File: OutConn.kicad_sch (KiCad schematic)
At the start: 0 parts

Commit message: Adding 5v and 3v3 buck
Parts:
- added J?: 2041441-1, TE_2041441-1, symbol 2041441-1:DP_CONN
- added J?: USB_A_Stacked, symbol Connector:USB_A_Stacked
- added R?: 5M, symbol Device:R_US
- added R?: 1M, symbol Device:R_US
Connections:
- new net: J?.14 (CFG2), R?.1
- new net: J?.13 (CFG1), R?.1
- new net +3V3: J?.20 (DP_PWR)
- new net +5V: J?.1 (VBUS1), J?.5 (VBUS2)
- new net GND: J?.11 (GND), J?.16 (GND), J?.19 (RTN), J?.2 (GND), J?.4 (GND1), J?.5 (GND), J?.8 (GND), J?.8 (GND2), J?.9 (Shield), J?.SH1 (SHIELD), J?.SH2 (SHIELD), J?.SH3 (SHIELD), R?.2, R?.2
- new net SINK_DP.AUX_M: J?.17 (AUX_N)
- new net SINK_DP.AUX_P: J?.15 (AUX_P)
- new net SINK_DP.D0_M: J?.3 (ML0_M)
- new net SINK_DP.D0_P: J?.1 (ML0_P)
- new net SINK_DP.D1_M: J?.6 (ML1_N)
- new net SINK_DP.D1_P: J?.4 (ML1_P)
- new net SINK_DP.D2_M: J?.9 (ML2_M)
- new net SINK_DP.D2_P: J?.7 (ML2_P)
- new net SINK_DP.D3_M: J?.12 (ML3_N)
- new net SINK_DP.D3_P: J?.10 (ML3_P)
- new net SINK_DP.HPD: J?.18 (HPD)
- new net UFP_USB1.D_M: J?.2 (D1-)
- new net UFP_USB1.D_P: J?.3 (D1+)
- new net UFP_USB2.D_M: J?.6 (D2-)
- new net UFP_USB2.D_P: J?.7 (D2+)

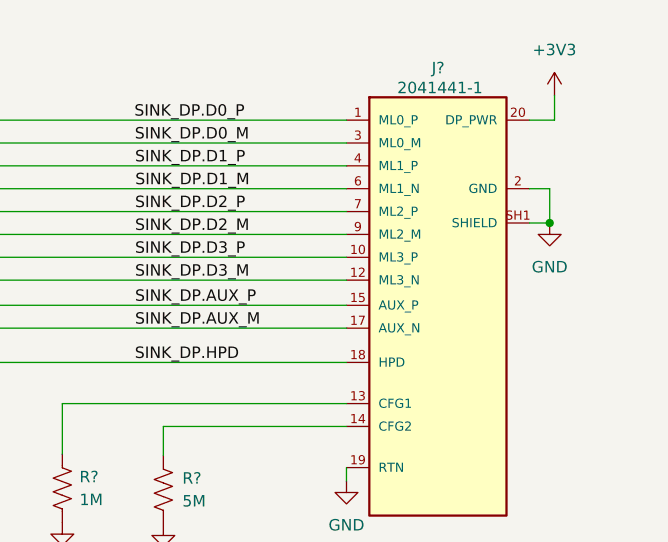
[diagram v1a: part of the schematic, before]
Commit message: fixing sheet numbers and adding schematic PDF
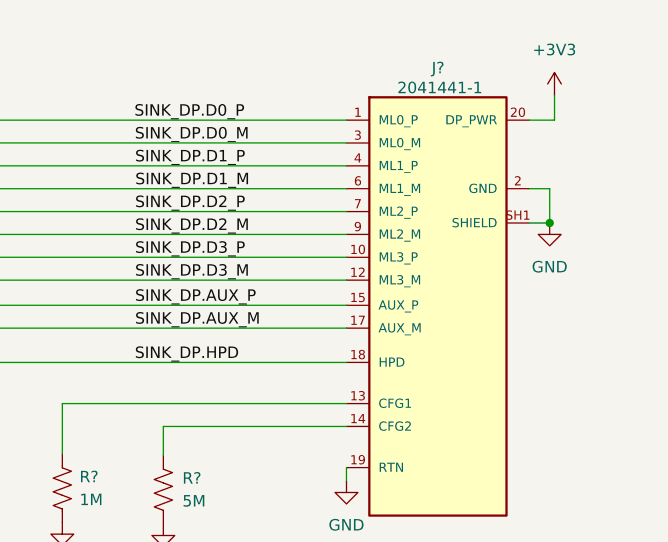
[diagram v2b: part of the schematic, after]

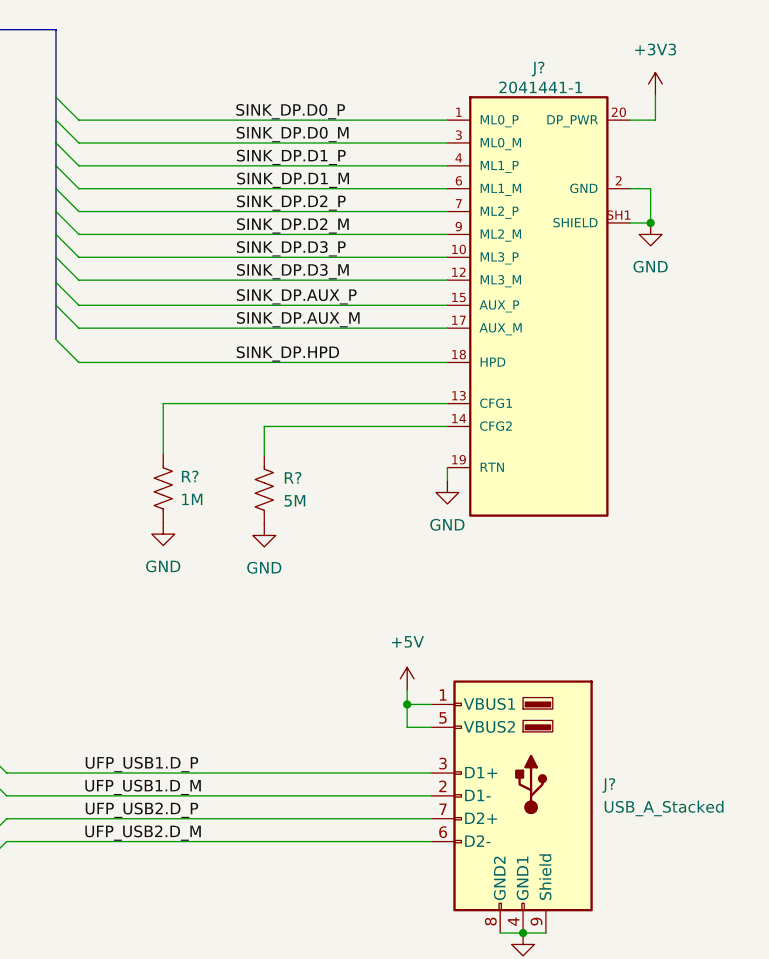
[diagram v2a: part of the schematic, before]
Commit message: Fixing ERC
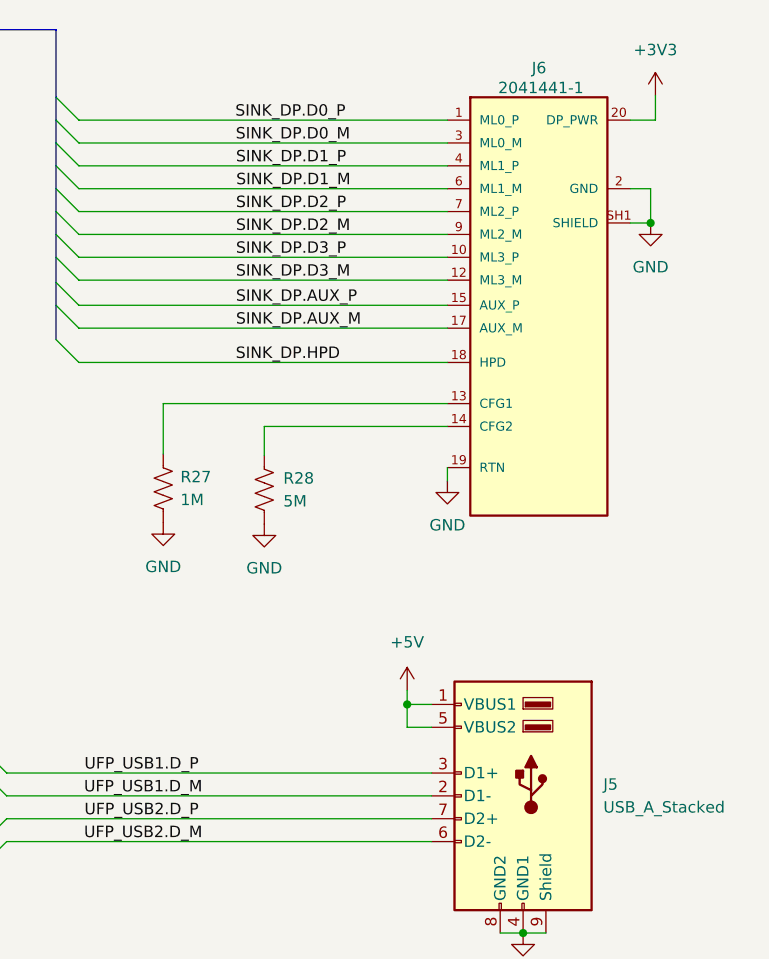
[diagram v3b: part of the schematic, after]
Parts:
- gave numbers to parts that had none: 4
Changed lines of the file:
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@@
   (symbol (lib_id "Device:R_US") (at 122.3518 117.4496 0) (unit 1)
     (in_bom yes) (on_board yes) (fields_autoplaced)
-    (property "Reference" "R?" (id 0) (at 124.46 116.1795 0)
+    (property "Reference" "R28" (id 0) (at 124.46 116.1795 0)
       (effects (font (size 1.27 1.27)) (justify left))
     )
@@
   (symbol (lib_id "power:+5V") (at 138.2268 139.7254 0) (unit 1)
     (in_bom yes) (on_board yes) (fields_autoplaced)
-    (property "Reference" "#PWR?" (id 0) (at 138.2268 143.5354 0)
+    (property "Reference" "#PWR050" (id 0) (at 138.2268 143.5354 0)
       (effects (font (size 1.27 1.27)) hide)
     )
@@
   (symbol (lib_id "power:GND") (at 151.1046 166.7002 0) (mirror y) (unit 1)
     (in_bom yes) (on_board yes) (fields_autoplaced)
-    (property "Reference" "#PWR?" (id 0) (at 151.1046 173.0502 0)
+    (property "Reference" "#PWR052" (id 0) (at 151.1046 173.0502 0)
       (effects (font (size 1.27 1.27)) hide)
     )
@@
   (symbol (lib_id "power:+3V3") (at 165.8112 73.6346 0) (unit 1)
     (in_bom yes) (on_board yes) (fields_autoplaced)
-    (property "Reference" "#PWR?" (id 0) (at 165.8112 77.4446 0)
+    (property "Reference" "#PWR054" (id 0) (at 165.8112 77.4446 0)
       (effects (font (size 1.27 1.27)) hide)
     )
@@
   (symbol (lib_id "2041441-1:DP_CONN") (at 152.8572 96.9518 0) (unit 1)
     (in_bom yes) (on_board yes)
-    (property "Reference" "J?" (id 0) (at 152.8826 70.5866 0))
+    (property "Reference" "J6" (id 0) (at 152.8826 70.5866 0))
     (property "Value" "2041441-1" (id 1) (at 153.0858 72.7964 0))
     (property "Footprint" "TE_2041441-1" (id 2) (at 152.8572 91.6178 0)
@@
   (symbol (lib_id "Device:R_US") (at 111.125 117.2972 0) (unit 1)
     (in_bom yes) (on_board yes) (fields_autoplaced)
-    (property "Reference" "R?" (id 0) (at 113.03 116.0271 0)
+    (property "Reference" "R27" (id 0) (at 113.03 116.0271 0)
       (effects (font (size 1.27 1.27)) (justify left))
     )
@@
   (symbol (lib_id "Connector:USB_A_Stacked") (at 151.1046 151.4602 0) (mirror y) (unit 1)
     (in_bom yes) (on_board yes) (fields_autoplaced)
-    (property "Reference" "J?" (id 0) (at 160.02 150.1901 0)
+    (property "Reference" "J5" (id 0) (at 160.02 150.1901 0)
       (effects (font (size 1.27 1.27)) (justify right))
     )
@@
   (symbol (lib_id "power:GND") (at 165.2778 87.8078 0) (unit 1)
     (in_bom yes) (on_board yes) (fields_autoplaced)
-    (property "Reference" "#PWR?" (id 0) (at 165.2778 94.1578 0)
+    (property "Reference" "#PWR053" (id 0) (at 165.2778 94.1578 0)
       (effects (font (size 1.27 1.27)) hide)
     )
@@
   (symbol (lib_id "power:GND") (at 122.3518 121.2596 0) (unit 1)
     (in_bom yes) (on_board yes) (fields_autoplaced)
-    (property "Reference" "#PWR?" (id 0) (at 122.3518 127.6096 0)
+    (property "Reference" "#PWR049" (id 0) (at 122.3518 127.6096 0)
       (effects (font (size 1.27 1.27)) hide)
     )
@@
   (symbol (lib_id "power:GND") (at 142.6972 116.4844 0) (unit 1)
     (in_bom yes) (on_board yes) (fields_autoplaced)
-    (property "Reference" "#PWR?" (id 0) (at 142.6972 122.8344 0)
+    (property "Reference" "#PWR051" (id 0) (at 142.6972 122.8344 0)
       (effects (font (size 1.27 1.27)) hide)
     )
@@
   (symbol (lib_id "power:GND") (at 111.125 121.1072 0) (unit 1)
     (in_bom yes) (on_board yes) (fields_autoplaced)
-    (property "Reference" "#PWR?" (id 0) (at 111.125 127.4572 0)
+    (property "Reference" "#PWR048" (id 0) (at 111.125 127.4572 0)
       (effects (font (size 1.27 1.27)) hide)
     )

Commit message: Pushing what i have now
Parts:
- removed J5: USB_A_Stacked, symbol Connector:USB_A_Stacked
- removed J6: 2041441-1, TE_2041441-1, symbol 2041441-1:DP_CONN
- removed R27: 1M, symbol Device:R_US
- removed R28: 5M, symbol Device:R_US
- added C31, C32: ${Capacitance}, Capacitor_SMD:C_0603_1608Metric_Pad1.08x0.95mm_HandSolder, symbol Rockerrobotics:Capacitors/1276-1034-1-ND
- added C? (x2): ${Capacitance}, Capacitor_SMD:C_0603_1608Metric_Pad1.08x0.95mm_HandSolder, symbol Rockerrobotics:Capacitors/1276-1935-1-ND
- added P3, P4: USB_C_Plug_USB2.0, Rockerrobotics:AMPHENOL_12402012E212A, symbol Rockerrobotics:Connectors/664-12402012E212ADKR-ND
- added R18, R19, R20, R21: ${Resistance}, Resistor_SMD:R_0805_2012Metric_Pad1.20x1.40mm_HandSolder, symbol Rockerrobotics:Resistors/13-RC0805FR-1322KLCT-ND
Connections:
- net GND: now also C31.2, C32.2, C?.2, C?.2, P3.A1 (GND), P3.A12 (GND), P3.B1 (GND), P3.B12 (GND), P3.S1 (SHIELD), P4.A1 (GND), P4.A12 (GND), P4.B1 (GND), P4.B12 (GND), P4.S1 (SHIELD)
- net UFP_USB1.D_P: now also P3.A6 (D+)
- net UFP_USB2.D_P: now also P4.A6 (D+)
- new net: P4.B5 (VCONN), R19.2
- new net: P3.B5 (VCONN), R18.2
- new net: P4.A5 (CC), R21.2
- new net: P3.A5 (CC), R20.2
- new net UFP_USB1.D_N: P3.A7 (D-)
- new net UFP_USB2.D_N: P4.A7 (D-)
- new net USP_PWR1: C31.1, C?.1, P3.A4 (VBUS), P3.A9 (VBUS), P3.B4 (VBUS), P3.B9 (VBUS), R18.1, R20.1
- new net USP_PWR2: C32.1, C?.1, P4.A4 (VBUS), P4.A9 (VBUS), P4.B4 (VBUS), P4.B9 (VBUS), R19.1, R21.1
